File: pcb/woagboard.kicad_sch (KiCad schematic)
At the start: 92 parts, among them J1 Battery JST, J2 Flash connection, J3 Battery JST, J4 Flash connection, SW10 SW_Push, SW11 SW_Push, SW12 SW_Push, SW13 SW_Push, SW14 SW_Push, SW15 SW_Push, SW16 SW_Push, SW17 SW_Push, SW18 SW_Push, SW19 SW_Push, SW20 SW_Push, SW21 SW_Push, SW22 SW_Push, SW23 SW_Push, SW24 SW_Push, SW25 SW_Push, SW26 SW_Push, SW27 SW_Push, SW28 SW_Push, SW29 SW_Push, SW3 SW_Push, SW30 SW_Push, SW31 SW_Push, SW32 SW_Push, SW33 SW_Push, SW34 SW_Push, SW35 SW_Push, SW36 SW_Push, SW4 SW_Push, SW5 SW_Push, SW6 SW_Push, SW7 SW_Push, SW8 SW_Push, SW9 SW_Push, U1 USBLC6-2, U2 USBLC6-2, U3 BQ24075, U4 BQ24075, U5 nRF52840_E73-2G4M08S1C, U9 nRF52840_E73-2G4M08S1C, Y1 32.768 KHz, Y2 32.768 KHz

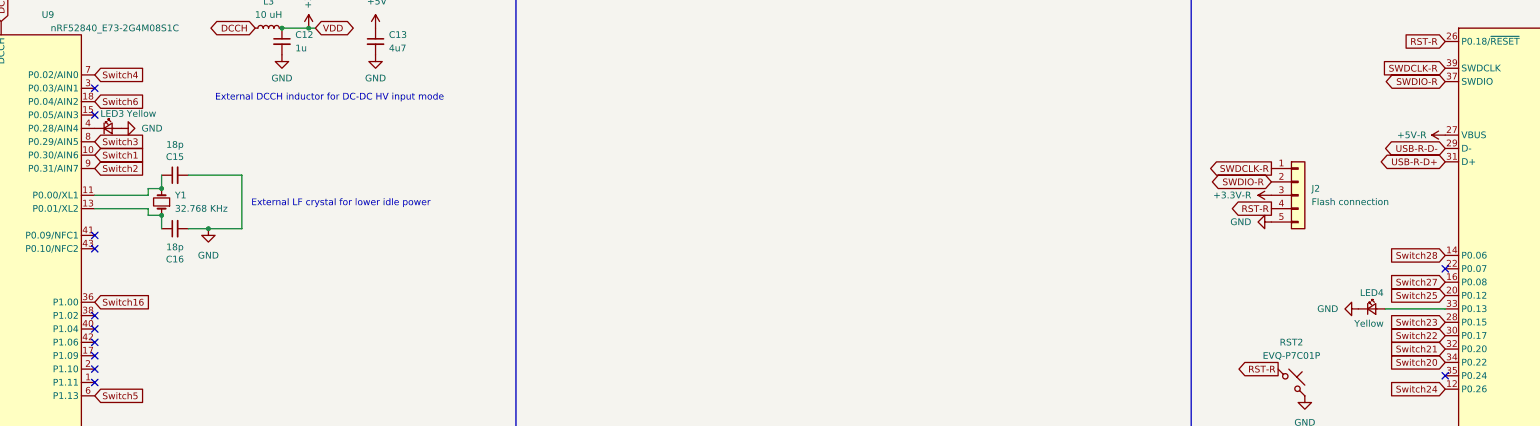
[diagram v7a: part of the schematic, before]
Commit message: feat: better grounding and positioning
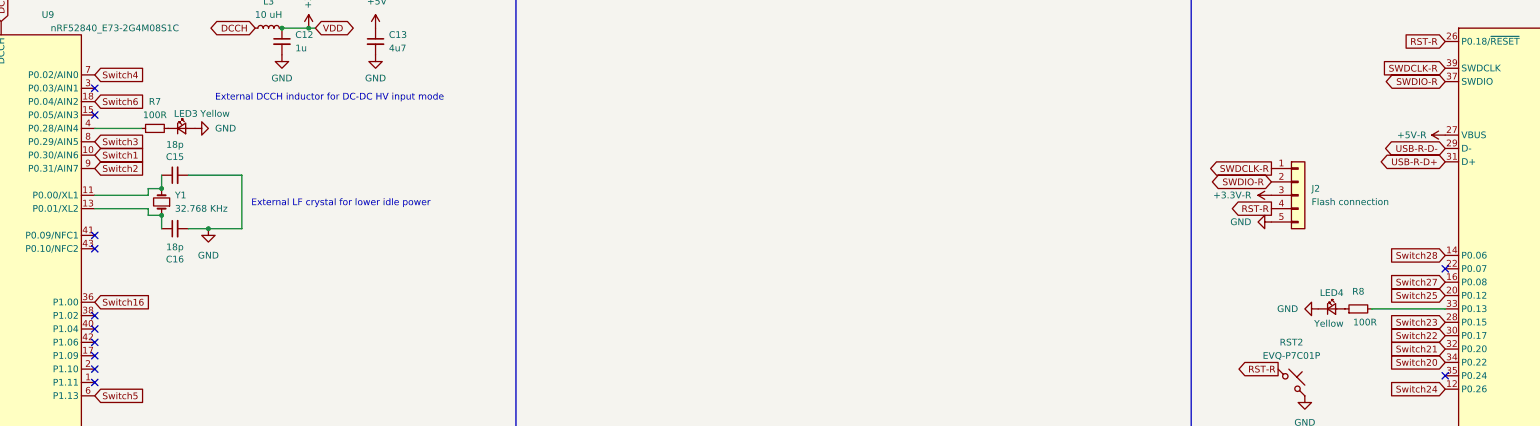
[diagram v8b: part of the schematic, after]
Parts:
- added R7, R8: 100R, Resistor_SMD:R_0402_1005Metric, symbol Device:R_Small
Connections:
- net at U9.4 (P0.28/AIN4): now also R7.1; no longer LED3.1 (K)
- net at LED4.2 (A): now also R8.1; no longer U5.33 (P0.13)
- new net: LED3.1 (K), R7.2
- new net: R8.2, U5.33 (P0.13)
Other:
- moved on the sheet: LED3, LED4
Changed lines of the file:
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@@
 	(wire
 		(pts
+			(xy 121.92 199.39) (xy 113.03 199.39)
+		)
+		(stroke
+			(width 0)
+			(type default)
+		)
+	)
+	(wire
+		(pts
 			(xy 342.9 140.97) (xy 359.41 140.97)
 		)
@@
 	(wire
 		(pts
-			(xy 358.14 233.68) (xy 369.57 233.68)
-		)
-		(stroke
-			(width 0)
-			(type default)
-		)
-	)
-	(wire
-		(pts
 			(xy 332.74 123.19) (xy 346.71 123.19)
 		)
@@
 	(wire
 		(pts
+			(xy 355.6 233.68) (xy 369.57 233.68)
+		)
+		(stroke
+			(width 0)
+			(type default)
+		)
+	)
+	(wire
+		(pts
 			(xy 81.28 116.84) (xy 81.28 118.11)
 		)
@@
 	)
 	(symbol
+		(lib_id "Device:R_Small")
+		(at 124.46 199.39 90)
+		(unit 1)
+		(exclude_from_sim no)
+		(in_bom yes)
+		(on_board yes)
+		(dnp no)
+		(fields_autoplaced yes)
+		(property "Reference" "R7"
+			(at 124.46 194.31 90)
+			(effects
+				(font
+					(size 1.27 1.27)
+				)
+			)
+		)
+		(property "Value" "100R"
+			(at 124.46 196.85 90)
+			(effects
+				(font
+					(size 1.27 1.27)
+				)
+			)
+		)
+		(property "Footprint" "Resistor_SMD:R_0402_1005Metric"
+			(at 124.46 199.39 0)
+			(effects
+				(font
+					(size 1.27 1.27)
+				)
+				(hide yes)
+			)
+		)
+		(property "Datasheet" "~"
+			(at 124.46 199.39 0)
+			(effects
+				(font
+					(size 1.27 1.27)
+				)
+				(hide yes)
+			)
+		)
+		(property "Description" "Resistor, small symbol"
+			(at 124.46 199.39 0)
+			(effects
+				(font
+					(size 1.27 1.27)
+				)
+				(hide yes)
+			)
+		)
+		(pin "2"
+		)
+		(pin "1"
+		)
+		(instances
+			(project ""
+				(path "/c2a65ddb-3915-4293-98a9-444287fe2a3d"
+					(reference "R7")
+					(unit 1)
+				)
+			)
+		)
+	)
+	(symbol
 		(lib_id "power:GND")
 		(at 44.45 121.92 270)
@@
 	(symbol
 		(lib_id "Device:LED_Small")
-		(at 355.6 233.68 0)
+		(at 347.98 233.68 0)
 		(unit 1)
 		(exclude_from_sim no)
@@
 		(dnp no)
 		(property "Reference" "LED4"
-			(at 357.886 230.632 0)
+			(at 350.266 230.632 0)
 			(effects
 				(font
@@
 		)
 		(property "Value" "Yellow"
-			(at 357.886 236.474 0)
+			(at 350.266 236.474 0)
 			(effects
 				(font
@@
 		)
 		(property "Footprint" "LED_SMD:LED_0805_2012Metric"
-			(at 355.6 233.68 90)
+			(at 347.98 233.68 90)
 			(effects
 				(font
@@
 		)
 		(property "Datasheet" "~"
-			(at 355.6 233.68 90)
+			(at 347.98 233.68 90)
 			(effects
 				(font
@@
 		)
 		(property "Description" "Light emitting diode, small symbol"
-			(at 355.6 233.68 0)
+			(at 347.98 233.68 0)
 			(effects
 				(font
@@
 	(symbol
 		(lib_id "power:GND")
-		(at 353.06 233.68 270)
+		(at 345.44 233.68 270)
 		(unit 1)
 		(exclude_from_sim no)
@@
 		(fields_autoplaced yes)
 		(property "Reference" "#PWR049"
-			(at 346.71 233.68 0)
+			(at 339.09 233.68 0)
 			(effects
 				(font
@@
 		)
 		(property "Value" "GND"
-			(at 349.25 233.6799 90)
+			(at 341.63 233.6799 90)
 			(effects
 				(font
@@
 		)
 		(property "Footprint" ""
-			(at 353.06 233.68 0)
+			(at 345.44 233.68 0)
 			(effects
 				(font
@@
 		)
 		(property "Datasheet" ""
-			(at 353.06 233.68 0)
+			(at 345.44 233.68 0)
 			(effects
 				(font
@@
 		)
 		(property "Description" "Power symbol creates a global label with name \"GND\" , ground"
-			(at 353.06 233.68 0)
+			(at 345.44 233.68 0)
 			(effects
 				(font
@@
 	(symbol
 		(lib_id "power:GND")
-		(at 118.11 199.39 90)
+		(at 132.08 199.39 90)
 		(unit 1)
 		(exclude_from_sim no)
@@
 		(fields_autoplaced yes)
 		(property "Reference" "#PWR03"
-			(at 124.46 199.39 0)
+			(at 138.43 199.39 0)
 			(effects
 				(font
@@
 		)
 		(property "Value" "GND"
-			(at 121.92 199.3899 90)
+			(at 135.89 199.3899 90)
 			(effects
 				(font
@@
 		)
 		(property "Footprint" ""
-			(at 118.11 199.39 0)
+			(at 132.08 199.39 0)
 			(effects
 				(font
@@
 		)
 		(property "Datasheet" ""
-			(at 118.11 199.39 0)
+			(at 132.08 199.39 0)
 			(effects
 				(font
@@
 		)
 		(property "Description" "Power symbol creates a global label with name \"GND\" , ground"
-			(at 118.11 199.39 0)
+			(at 132.08 199.39 0)
 			(effects
 				(font
@@
 	)
 	(symbol
+		(lib_id "Device:R_Small")
+		(at 353.06 233.68 90)
+		(unit 1)
+		(exclude_from_sim no)
+		(in_bom yes)
+		(on_board yes)
+		(dnp no)
+		(property "Reference" "R8"
+			(at 353.06 230.378 90)
+			(effects
+				(font
+					(size 1.27 1.27)
+				)
+			)
+		)
+		(property "Value" "100R"
+			(at 354.33 236.22 90)
+			(effects
+				(font
+					(size 1.27 1.27)
+				)
+			)
+		)
+		(property "Footprint" "Resistor_SMD:R_0402_1005Metric"
+			(at 353.06 233.68 0)
+			(effects
+				(font
+					(size 1.27 1.27)
+				)
+				(hide yes)
+			)
+		)
+		(property "Datasheet" "~"
+			(at 353.06 233.68 0)
+			(effects
+				(font
+					(size 1.27 1.27)
+				)
+				(hide yes)
+			)
+		)
+		(property "Description" "Resistor, small symbol"
+			(at 353.06 233.68 0)
+			(effects
+				(font
+					(size 1.27 1.27)
+				)
+				(hide yes)
+			)
+		)
+		(pin "2"
+		)
+		(pin "1"
+		)
+		(instances
+			(project "woagboard"
+				(path "/c2a65ddb-3915-4293-98a9-444287fe2a3d"
+					(reference "R8")
+					(unit 1)
+				)
+			)
+		)
+	)
+	(symbol
 		(lib_id "power:GND")
 		(at 405.13 327.66 0)
@@
 	(symbol
 		(lib_id "Device:LED_Small")
-		(at 115.57 199.39 0)
+		(at 129.54 199.39 0)
 		(unit 1)
 		(exclude_from_sim no)
@@
 		(dnp no)
 		(property "Reference" "LED3"
-			(at 118.618 196.596 0)
+			(at 132.588 196.596 0)
 			(effects
 				(font
@@
 		)
 		(property "Value" "Yellow"
-			(at 124.714 196.596 0)
+			(at 138.684 196.596 0)
 			(effects
 				(font
@@
 		)
 		(property "Footprint" "LED_SMD:LED_0805_2012Metric"
-			(at 115.57 199.39 90)
+			(at 129.54 199.39 90)
 			(effects
 				(font
@@
 		)
 		(property "Datasheet" "~"
-			(at 115.57 199.39 90)
+			(at 129.54 199.39 90)
 			(effects
 				(font
@@
 		)
 		(property "Description" "Light emitting diode, small symbol"
-			(at 115.57 199.39 0)
+			(at 129.54 199.39 0)
 			(effects
 				(font
